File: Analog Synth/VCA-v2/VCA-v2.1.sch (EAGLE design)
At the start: 43 parts, among them IC2 TL084D, T1 DMMT3904W, T2 MMBT2222ALT1

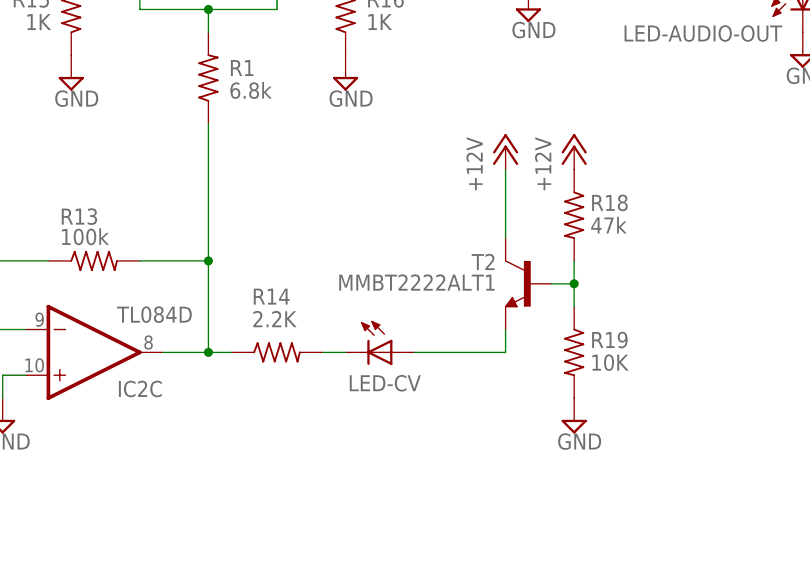
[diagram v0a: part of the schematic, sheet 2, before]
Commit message: ScreamFilter v1.0; TODO: Add LEDs to ScreamFilter...   updated VCA-v2 for some reason.
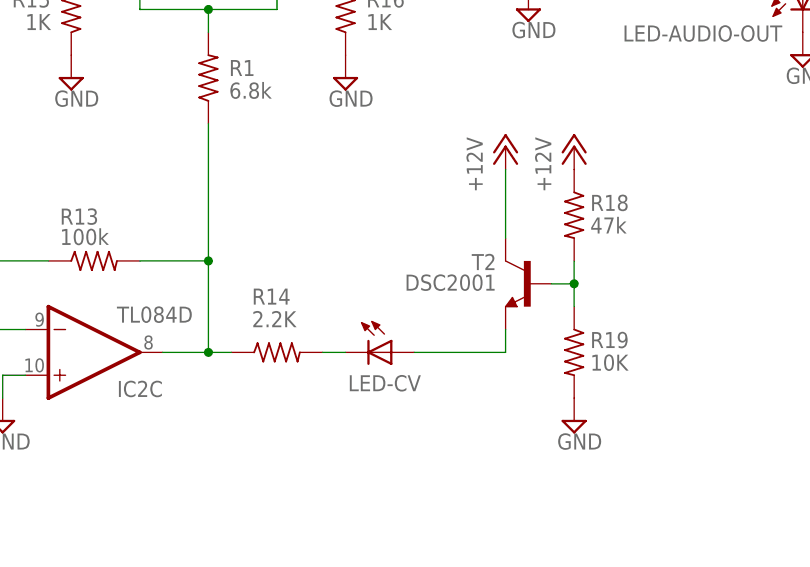
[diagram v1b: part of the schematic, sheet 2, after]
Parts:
- T2: value MMBT2222ALT1 -> DSC2001
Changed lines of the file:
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@@
 <part name="SUPPLY17" library="supply2" deviceset="GND" device=""/>
 <part name="T1" library="!synth_sch" deviceset="DMMT3904W" device=""/>
-<part name="T2" library="transistor" deviceset="*-NPN-" device="SOT23-BEC" technology="MMBT2222ALT1" value="MMBT2222ALT1"/>
+<part name="T2" library="transistor" deviceset="*-NPN-" device="SOT23-BEC" technology="MMBT2222ALT1" value="DSC2001"/>
 </parts>
 <sheets>
